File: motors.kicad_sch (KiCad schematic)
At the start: 6 parts, among them J3 Conn_01x02, J4 Conn_01x02, J5 Conn_01x02, J6 Conn_01x02, U5 TB6612FNG, U6 TB6612FNG

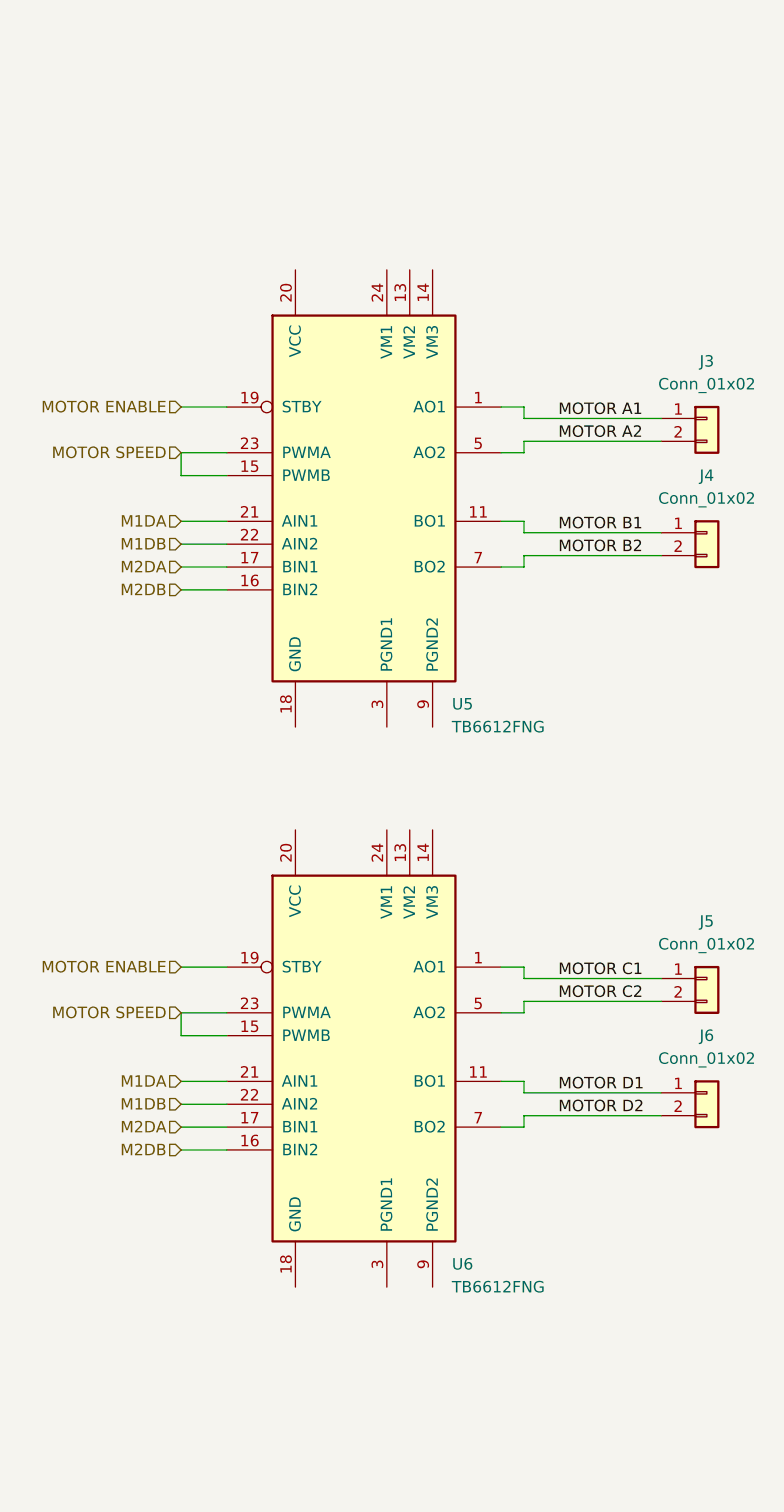
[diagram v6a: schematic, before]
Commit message: feat: finalized connections to the motor driver ICs
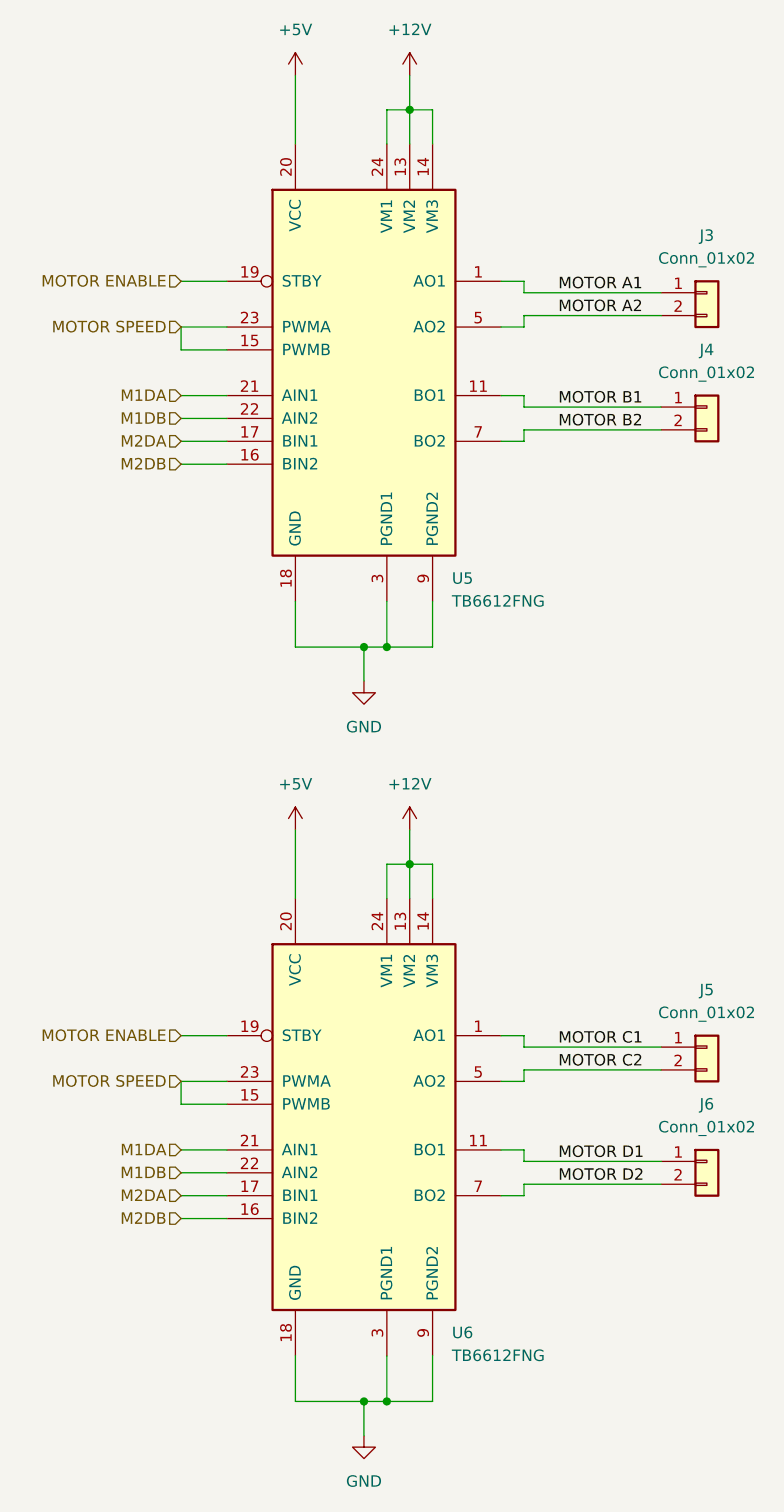
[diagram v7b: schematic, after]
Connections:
- net GND: now reaches U6.10 (PGND2), U6.9 (PGND2)
- net GND: now also U5.10 (PGND2), U5.18 (GND), U5.3 (PGND1), U5.4 (PGND1), U5.9 (PGND2), U6.18 (GND), U6.3 (PGND1), U6.4 (PGND1)
- net +12V: now reaches U6.13 (VM2)
- net +12V: now also U5.13 (VM2), U5.14 (VM3), U5.24 (VM1), U6.14 (VM3), U6.24 (VM1)
- net +5V: now reaches U6.20 (VCC)
- net +5V: now also U5.20 (VCC)
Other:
- moved on the sheet: J3, J4, J5, J6, U5, U6

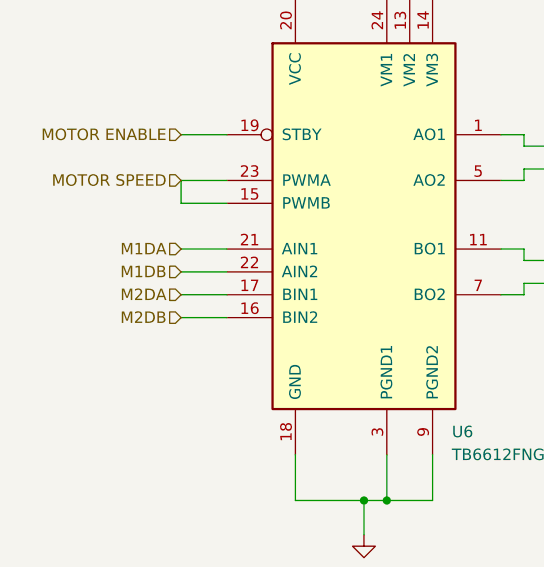
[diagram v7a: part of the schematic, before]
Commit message: feat: wired up audio system
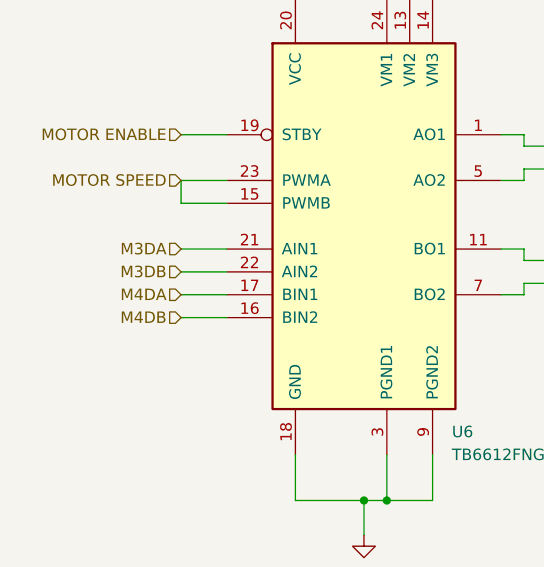
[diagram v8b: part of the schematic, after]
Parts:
- J3, J4, J5, J6: now left out of the parts list
- U5, U6: Part# (none) -> C141517
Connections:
- net M1DA: no longer U6.21 (AIN1)
- net M1DB: no longer U6.22 (AIN2)
- net M2DA: no longer U6.17 (BIN1)
- net M2DB: no longer U6.16 (BIN2)
- new net M3DA: U6.21 (AIN1)
- new net M3DB: U6.22 (AIN2)
- new net M4DA: U6.17 (BIN1)
- new net M4DB: U6.16 (BIN2)
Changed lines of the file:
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@@
+		)
+	)
+	(hierarchical_label "M3DA"
+		(shape input)
+		(at 110.49 143.51 180)
+		(effects
+			(font
+				(size 1.27 1.27)
+			)
+			(justify right)
+		)
+	)
+	(hierarchical_label "MOTOR ENABLE"
+		(shape input)
+		(at 110.49 130.81 180)
+		(effects
+			(font
+				(size 1.27 1.27)
+			)
+			(justify right)
+		)
+	)
+	(hierarchical_label "MOTOR SPEED"
+		(shape input)
+		(at 110.49 135.89 180)
+		(effects
+			(font
+				(size 1.27 1.27)
+			)
+			(justify right)
+		)
+	)
+	(hierarchical_label "M3DB"
+		(shape input)
+		(at 110.49 146.05 180)
+		(effects
+			(font
+				(size 1.27 1.27)
+			)
+			(justify right)
+		)
+	)
+	(hierarchical_label "M1DA"
+		(shape input)
+		(at 110.49 59.69 180)
+		(effects
+			(font
+				(size 1.27 1.27)
+			)
+			(justify right)
 		)
 	)
 	(hierarchical_label "M2DA"
 		(shape input)
+		(at 110.49 64.77 180)
+		(effects
+			(font
+				(size 1.27 1.27)
+			)
+			(justify right)
+		)
+	)
+	(hierarchical_label "M4DA"
+		(shape input)
 		(at 110.49 148.59 180)
 		(effects
@@
 		)
 	)
-	(hierarchical_label "MOTOR ENABLE"
-		(shape input)
-		(at 110.49 130.81 180)
+	(hierarchical_label "M1DB"
+		(shape input)
+		(at 110.49 62.23 180)
 		(effects
 			(font
@@
 	(hierarchical_label "MOTOR SPEED"
 		(shape input)
-		(at 110.49 135.89 180)
-		(effects
-			(font
-				(size 1.27 1.27)
-			)
-			(justify right)
-		)
-	)
-	(hierarchical_label "M1DB"
-		(shape input)
-		(at 110.49 146.05 180)
-		(effects
-			(font
-				(size 1.27 1.27)
-			)
-			(justify right)
-		)
-	)
-	(hierarchical_label "M1DA"
-		(shape input)
-		(at 110.49 59.69 180)
-		(effects
-			(font
-				(size 1.27 1.27)
-			)
-			(justify right)
-		)
-	)
-	(hierarchical_label "M2DA"
-		(shape input)
-		(at 110.49 64.77 180)
-		(effects
-			(font
-				(size 1.27 1.27)
-			)
-			(justify right)
-		)
-	)
-	(hierarchical_label "M1DA"
-		(shape input)
-		(at 110.49 143.51 180)
+		(at 110.49 52.07 180)
 		(effects
 			(font
@@
 	(hierarchical_label "M2DB"
 		(shape input)
+		(at 110.49 67.31 180)
+		(effects
+			(font
+				(size 1.27 1.27)
+			)
+			(justify right)
+		)
+	)
+	(hierarchical_label "M4DB"
+		(shape input)
 		(at 110.49 151.13 180)
-		(effects
-			(font
-				(size 1.27 1.27)
-			)
-			(justify right)
-		)
-	)
-	(hierarchical_label "M1DB"
-		(shape input)
-		(at 110.49 62.23 180)
-		(effects
-			(font
-				(size 1.27 1.27)
-			)
-			(justify right)
-		)
-	)
-	(hierarchical_label "MOTOR SPEED"
-		(shape input)
-		(at 110.49 52.07 180)
-		(effects
-			(font
-				(size 1.27 1.27)
-			)
-			(justify right)
-		)
-	)
-	(hierarchical_label "M2DB"
-		(shape input)
-		(at 110.49 67.31 180)
 		(effects
 			(font
@@
 		(unit 1)
 		(exclude_from_sim no)
-		(in_bom yes)
+		(in_bom no)
 		(on_board yes)
 		(dnp no)
@@
 		)
 		(property "Description" "Generic connector, single row, 01x02, script generated (kicad-library-utils/schlib/autogen/connector/)"
+			(at 168.91 60.96 0)
+			(effects
+				(font
+					(size 1.27 1.27)
+				)
+				(hide yes)
+			)
+		)
+		(property "Part#" ""
 			(at 168.91 60.96 0)
 			(effects
@@
 			)
 		)
+		(property "Part#" "C141517"
+			(at 130.81 140.97 0)
+			(effects
+				(font
+					(size 1.27 1.27)
+				)
+				(hide yes)
+			)
+		)
 		(pin "1"
 		)
@@
 		(unit 1)
 		(exclude_from_sim no)
-		(in_bom yes)
+		(in_bom no)
 		(on_board yes)
 		(dnp no)
@@
 		)
 		(property "Description" "Generic connector, single row, 01x02, script generated (kicad-library-utils/schlib/autogen/connector/)"
+			(at 168.91 48.26 0)
+			(effects
+				(font
+					(size 1.27 1.27)
+				)
+				(hide yes)
+			)
+		)
+		(property "Part#" ""
 			(at 168.91 48.26 0)
 			(effects
@@
 			)
 		)
+		(property "Part#" "C141517"
+			(at 130.81 57.15 0)
+			(effects
+				(font
+					(size 1.27 1.27)
+				)
+				(hide yes)
+			)
+		)
 		(pin "1"
 		)
@@
 		(unit 1)
 		(exclude_from_sim no)
-		(in_bom yes)
+		(in_bom no)
 		(on_board yes)
 		(dnp no)
@@
 		)
 		(property "Description" "Generic connector, single row, 01x02, script generated (kicad-library-utils/schlib/autogen/connector/)"
+			(at 168.91 144.78 0)
+			(effects
+				(font
+					(size 1.27 1.27)
+				)
+				(hide yes)
+			)
+		)
+		(property "Part#" ""
 			(at 168.91 144.78 0)
 			(effects
@@
 		(unit 1)
 		(exclude_from_sim no)
-		(in_bom yes)
+		(in_bom no)
 		(on_board yes)
 		(dnp no)
@@
 			(at 168.91 132.08 0)
 			(effects
+				(font
+					(size 1.27 1.27)
+				)
+				(hide yes)
+			)
+		)
+		(property "Part#" ""
+			(at 168.91 132.08 0)
+			(effects
